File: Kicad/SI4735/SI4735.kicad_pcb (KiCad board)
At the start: 4 copper layers, 41.6 x 42.2 mm, 128 parts, among them IC1 SI4732-A10-GS, IC2 TCA9537DGSR, J1 Conn_01x03, J2 Conn_01x05, J3 Headphones, J5 DISP LEFT, J6 DISP RIGHT, J7 Conn_01x02_Pin, J8 TYPE-C-31-M-12, J9 Conn_01x02_Pin, Q2 2N7002, Q3 2SK508G-K51-AE3-R, SW1 SW_Push, T1 TestPoint, T10 TestPoint, T11 TestPoint, T5 TestPoint, T6 TestPoint, T7 TestPoint, T8 TestPoint, T9 TestPoint, U1 HT-CT62, U11 RT9013, U2 BME690, U4 LSM6DS3, U5 TPA6130A2RTJTR, U6 RT9013, U7 MAX98357AETE+T, U8 MAX98357AETE+T, U9 Si4735-D60-GU, X1 X322525MMB4SI, Y1 Si5351A-B-GT, Y2 RV-3032-C7

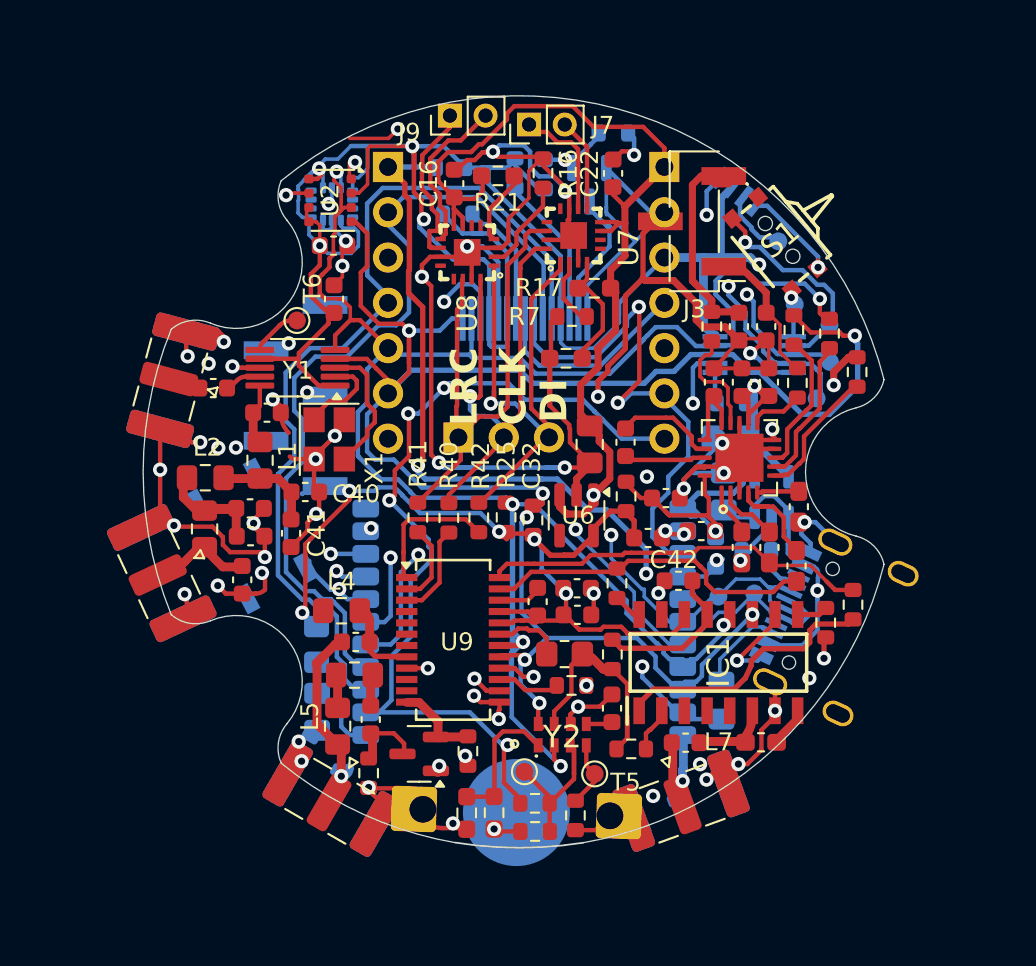
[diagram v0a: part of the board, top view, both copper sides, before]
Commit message: Add files via upload
- Rotation of SI4732 Radio
- Added Battery Charging IC TP4057
- Added Light Sensor VEML7700
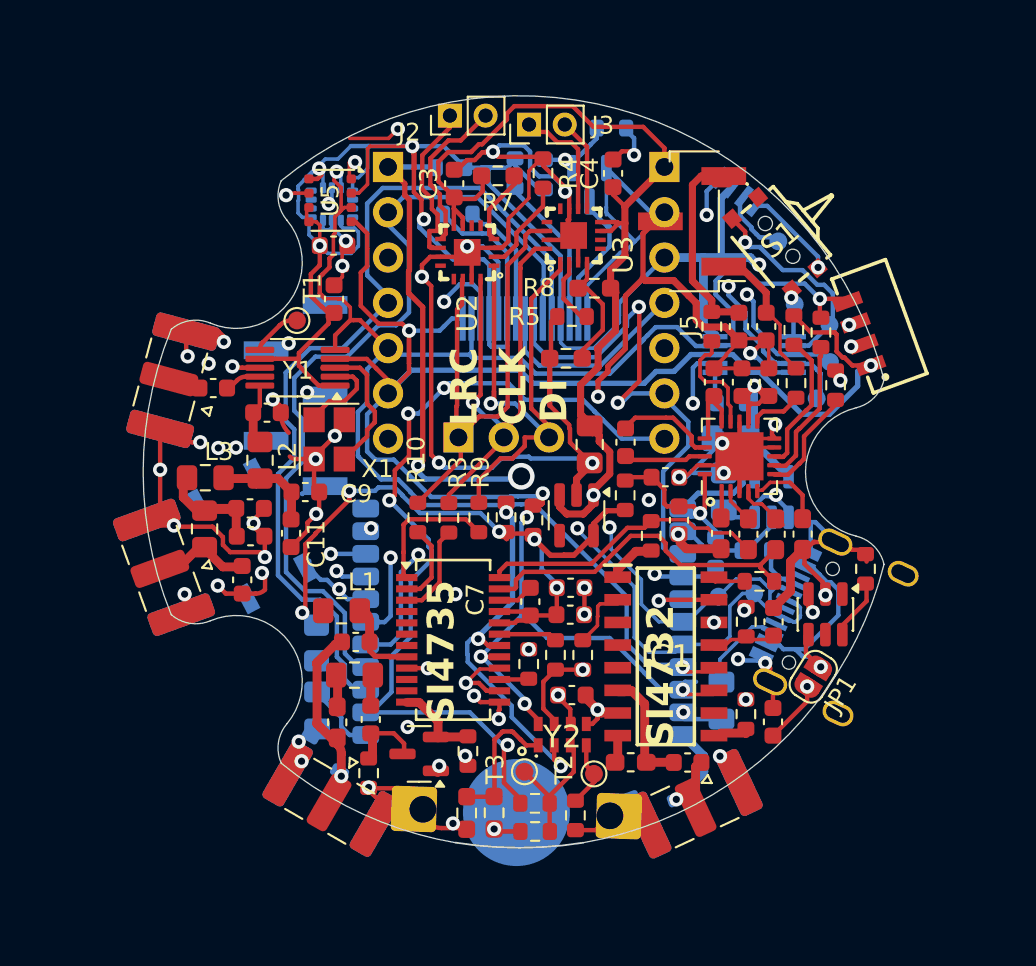
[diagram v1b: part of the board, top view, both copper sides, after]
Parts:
- removed the C33 at (106.7, 103.9)
- added C10: 1uF, Capacitor_SMD:C_0603_1608Metric, F.Cu at (113.7, 114.2)
- added IC2: VEML7700-TR, VEML7700:VEML7700, F.Cu at (119.4, 95.7)
- added JP1: Jumper_2_Small_Open, Jumper:SolderJumper-2_P1.3mm_Open_RoundedPad1.0x1.5mm, F.Cu at (116.0, 111.6)
- added R41: 2k, Resistor_SMD:R_0603_1608Metric, F.Cu at (118.9, 105.6)
- added U12: TP4057, Package_TO_SOT_SMD:TSOT-23-6, F.Cu at (116.7, 108.1)
- C30: renamed from C34; value 270p -> 330pF
- C33: renamed from C39; value 270p -> 330pF
- L5: footprint Inductor_SMD:L_0805_2012Metric_Pad1.15x1.40mm_HandSolder -> Inductor_SMD:L_0603_1608Metric_Pad1.05x0.95mm_HandSolder
- Q2: value 2N7002 -> SI2302
- R18: renamed from R38; value 2k -> 0R
- R2: renamed from R46; footprint Resistor_SMD:R_0805_2012Metric_Pad1.20x1.40mm_HandSolder -> Resistor_SMD:R_0603_1608Metric
- moved R19 12.0 mm to (106.9, 103.7)
- moved R28 7.99 mm to (113.0, 106.3), turned to 0 degrees
- moved R31 7.73 mm to (112.2, 108.6), turned to 90 degrees
- moved L7 7.40 mm to (105.8, 116.4), turned to 0 degrees
- moved R29 6.81 mm to (112.2, 113.7), turned to -90 degrees
- moved R18 5.93 mm to (103.1, 110.4), turned to 90 degrees
- moved C32 5.81 mm to (113.8, 108.6), turned to -90 degrees
- moved IC1 2.97 mm to (107.7, 110.5), turned to 0 degrees
- moved R1 2.68 mm to (100.0, 110.9), turned to -90 degrees
- moved C26 2.37 mm to (102.5, 112.7), turned to 0 degrees
- moved C14 2.13 mm to (113.9, 103.7)
- moved C15 1.55 mm to (115.4, 103.6)
- moved R13 1.42 mm to (117.2, 95.3)
- moved C12 1.40 mm to (110.8, 103.6)
- moved C13 1.39 mm to (112.4, 103.7)
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- renumbered ANT0 to ANT2, ANT5 to ANT3, C49 to C1, C41 to C11, C8 to C12, C9 to C13, C10 to C14, C11 to C15, C43 to C16, C46 to C17, C48 to C18, C47 to C19, C44 to C2, C14 to C20, C15 to C21, C18 to C22, C19 to C23, C20 to C24, C21 to C25, C23 to C26, C24 to C28, C16 to C3, C37 to C31, C42 to C32, C28 to C34, C45 to C35, C29 to C36, C30 to C37, C22 to C4, C38 to C5, C17 to C6, C32 to C7, C36 to C8, C40 to C9, D7 to D1, D6 to D2, D2 to D3, IC2 to IC3, J9 to J2, J7 to J3, J8 to J4, J3 to J5, J2 to J6, J5 to J7, J6 to J8, L4 to L1, L1 to L2, L2 to L3, L6 to L4, L3 to L6, Q3 to Q1, R45 to R1, R41 to R10, R50 to R11, R48 to R12, R1 to R13, R24 to R14, R49 to R15, R51 to R16, R25 to R17, R23 to R19, R15 to R20, R27 to R21, R13 to R22, R12 to R23, R8 to R24, R9 to R25, R10 to R26, R11 to R27, R39 to R29, R40 to R3, R22 to R30, R26 to R31, R18 to R32, R19 to R33, R44 to R35, R2 to R36, R53 to R37, R20 to R38, R52 to R39, R16 to R4, R47 to R40, R7 to R5, R14 to R6, R21 to R7, R17 to R8, R42 to R9, T6 to T1, T5 to T2, T11 to T3, T1 to T4, T7 to T5, T8 to T6, T9 to T7, T10 to T8, U9 to U1, U4 to U10, U8 to U2, U7 to U3, U5 to U4, U2 to U5, U13 to U6, U6 to U7, U1 to U8, U11 to U9
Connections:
- J4 pad A4: +5V -> +5VD
- J4 pad A9: +5V -> +5VD
- J4 pad B4: +5V -> +5VD
- J4 pad B9: +5V -> +5VD
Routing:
- net +5VD: track 0.00 -> 14.9 mm, vias 0 -> 1
- net Net-(IC1-LOUT/DFS): track 15.1 -> 2.77 mm
- net GND: track 259.4 -> 265.3 mm, vias 63 -> 61
- net L: track 21.8 -> 16.3 mm
- net Net-(IC1-RCLK): track 8.83 -> 3.57 mm
- net D+: track 43.3 -> 47.0 mm
- net Net-(IC1-AMI): track 4.70 -> 1.23 mm
- net +5V: track 89.9 -> 93.3 mm, vias 2 -> 4
- net OSC: track 13.2 -> 16.3 mm, vias 0 -> 2
- net IO9: track 29.5 -> 32.6 mm
- net +3V3: track 70.3 -> 67.2 mm, vias 7 -> 8
- net Net-(U12-PROG): track 0.00 -> 3.07 mm
- net Net-(U4-RIGHTINP): track 5.52 -> 3.29 mm
- net Net-(IC1-FMI): track 5.06 -> 7.07 mm
- net Net-(U4-RIGHTINM): track 2.36 -> 4.34 mm
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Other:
- board text added: "SI4732"
- board text added: "SI4735"

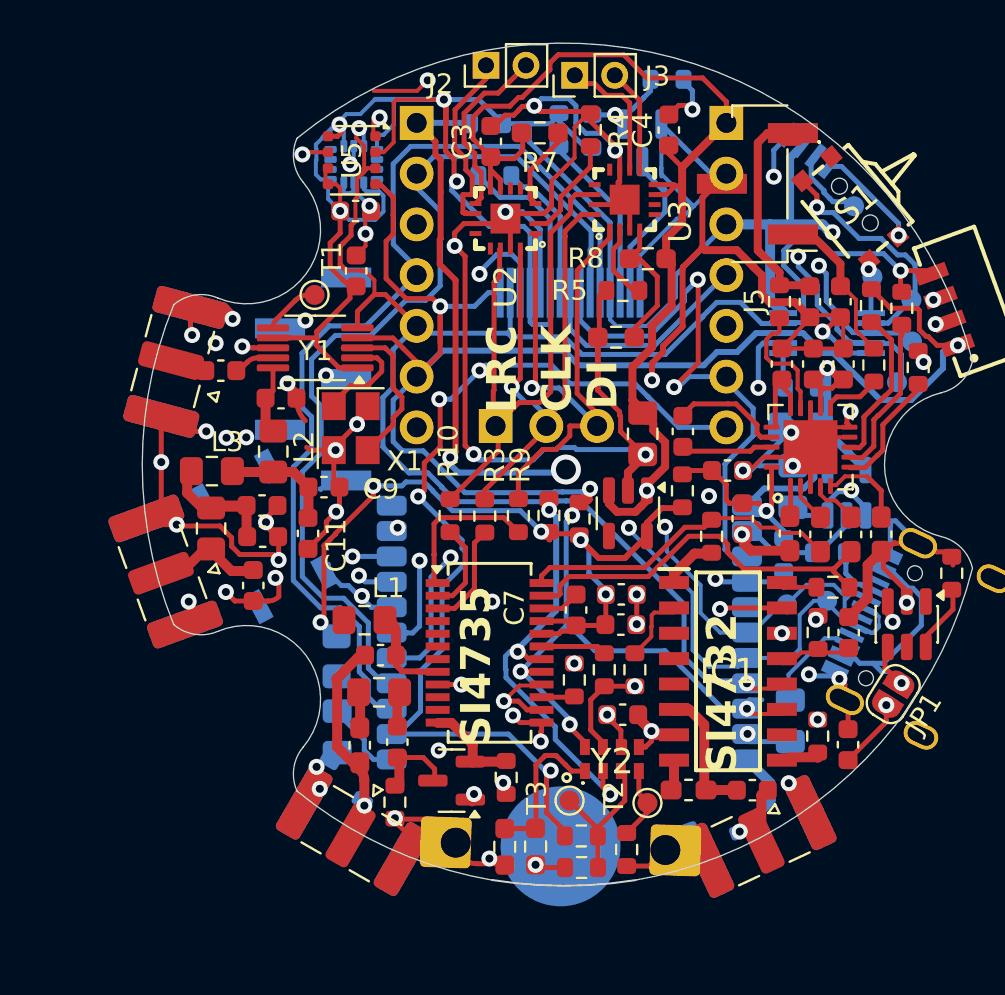
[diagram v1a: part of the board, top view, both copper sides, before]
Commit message: Add files via upload
- Added MLX90640 Thermal Camera
- Refinement of inner Layers to enhance EMC
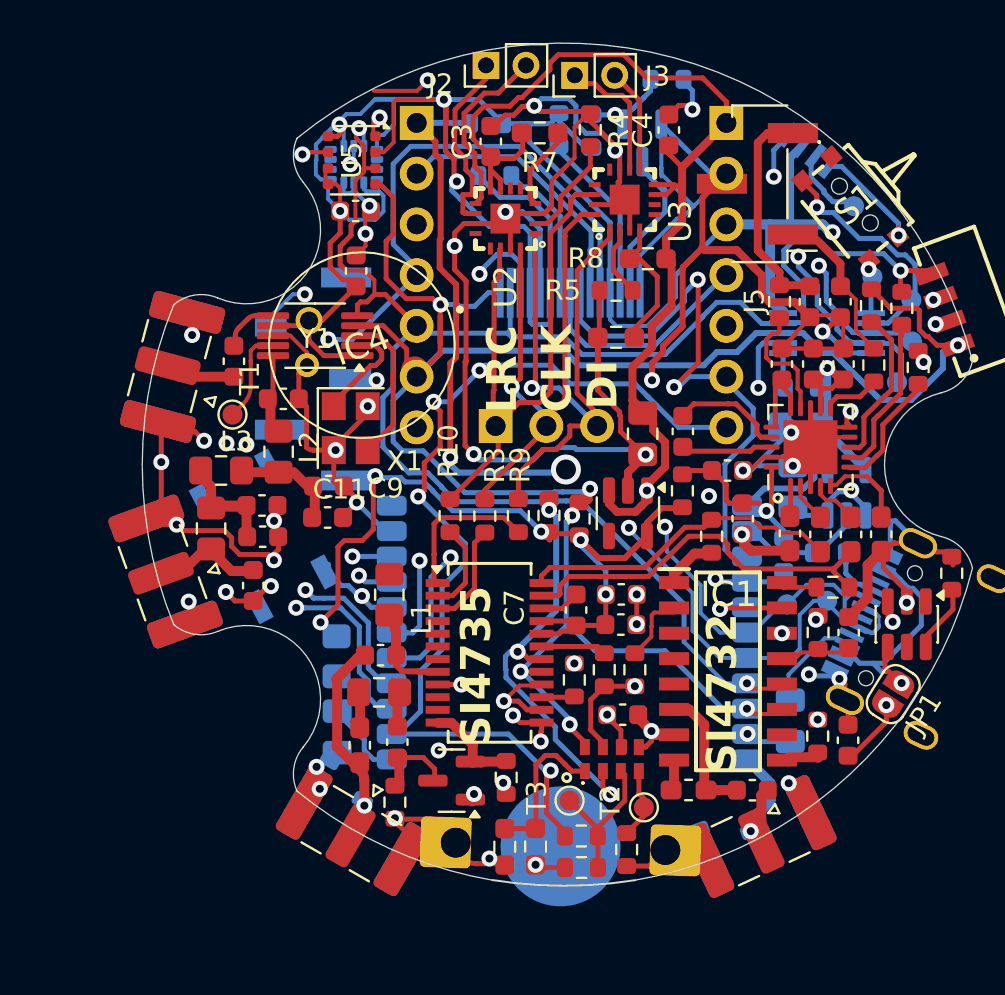
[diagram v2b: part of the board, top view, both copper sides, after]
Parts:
- added IC4: MLX90640ESF-BAB-000-SP, MLX90640:MLX90640ESFBAB000SP, F.Cu at (92.2, 93.2)
- IC2: value VEML7700-TR -> VEML7700
- moved T1 7.26 mm to (82.9, 97.7)
- moved L1 1.78 mm to (90.8, 106.7), turned to -90 degrees
- moved C11 1.26 mm to (87.7, 102.8), turned to 0 degrees
- moved C6 0.81 mm to (83.0, 95.0), turned to 90 degrees
- moved Y1 0.61 mm to (87.1, 93.7)
- moved D2 0.55 mm to (107.7, 118.9)
- moved L3 0.46 mm to (82.4, 100.5)
- moved R5 0.34 mm to (102.1, 91.4)
- moved ANT1 0.30 mm to (79.7, 95.2)
- moved T2 0.28 mm to (103.5, 117.3)
- moved L2 0.27 mm to (85.2, 99.5)
- moved C9 0.24 mm to (87.7, 101.2)
- moved C10 0.22 mm to (113.7, 114.0)
- moved C5 0.12 mm to (85.5, 96.9)
- turned R26 to -90 degrees
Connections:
- C6 pad 2: Net-(Y1-CLK1) -> Net-(Y1-CLK2)
- R26 pad 1: Net-(U4-HPRIGHT) -> Net-(J5-Pin_1)
- R26 pad 2: Net-(J5-Pin_1) -> Net-(U4-HPRIGHT)
- T1 pad 1: Net-(Y1-CLK2) -> Net-(Y1-CLK1)
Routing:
- net D+: track 47.0 -> 55.0 mm
- net SCL: track 115.7 -> 120.2 mm
- net Net-(ANT1-A): track 0.00 -> 4.26 mm
- net D-: track 39.4 -> 36.3 mm
- net Net-(Y1-CLK1): track 2.32 -> 4.87 mm
- net LCD_CS: track 47.3 -> 49.8 mm, vias 0 -> 1
- net +3.3VA: track 160.9 -> 162.5 mm
- net Net-(C11-Pad1): track 5.95 -> 4.82 mm
- net SDA: track 108.5 -> 107.4 mm
- net LORA_BUSY: track 37.0 -> 38.1 mm
- net +3V3: track 67.2 -> 68.2 mm
- net LCD_DC: track 50.4 -> 51.4 mm, vias 0 -> 2
- net BUT2: track 73.1 -> 73.9 mm
- net Net-(J5-Pin_3): track 11.8 -> 11.0 mm
- net Net-(Y1-CLK0): track 3.48 -> 3.99 mm
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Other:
- board text added: "D+"
- board text added: "D-"
- board text added: "F0"
- board text added: "G"
- board text added: "RAW 2"
- board text removed: "RAW"
